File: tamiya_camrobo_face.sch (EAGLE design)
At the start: 21 parts, among them J4 AUDIO_JACK_3.5MM_KIT

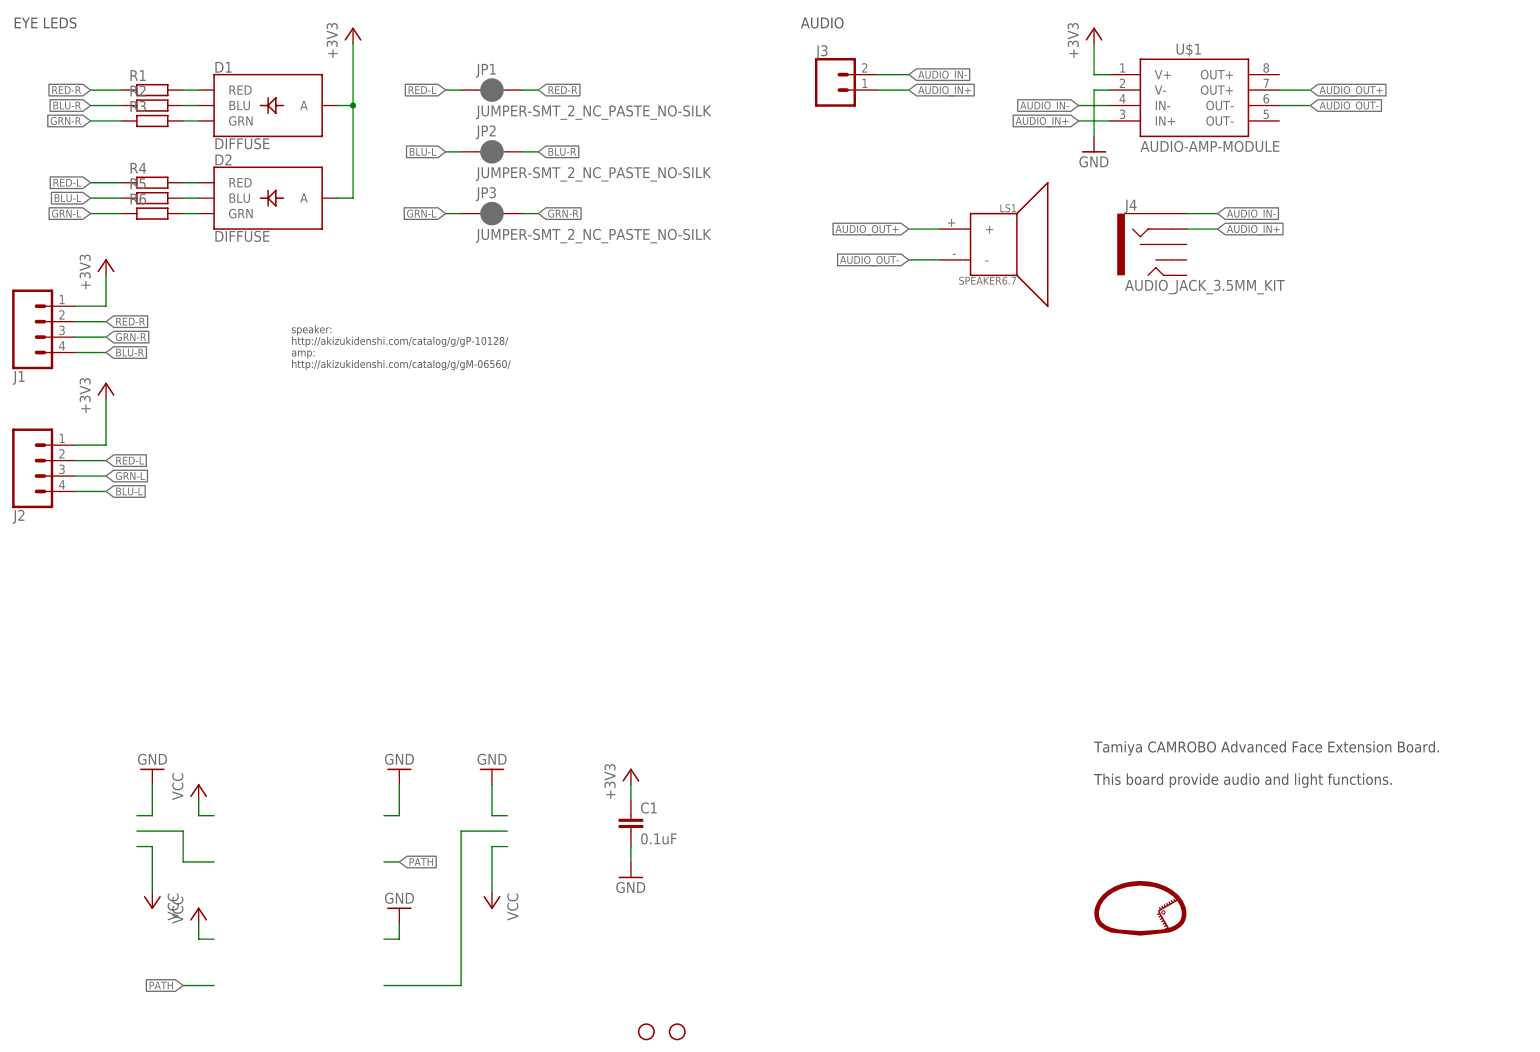
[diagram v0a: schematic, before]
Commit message: exchange led and amp
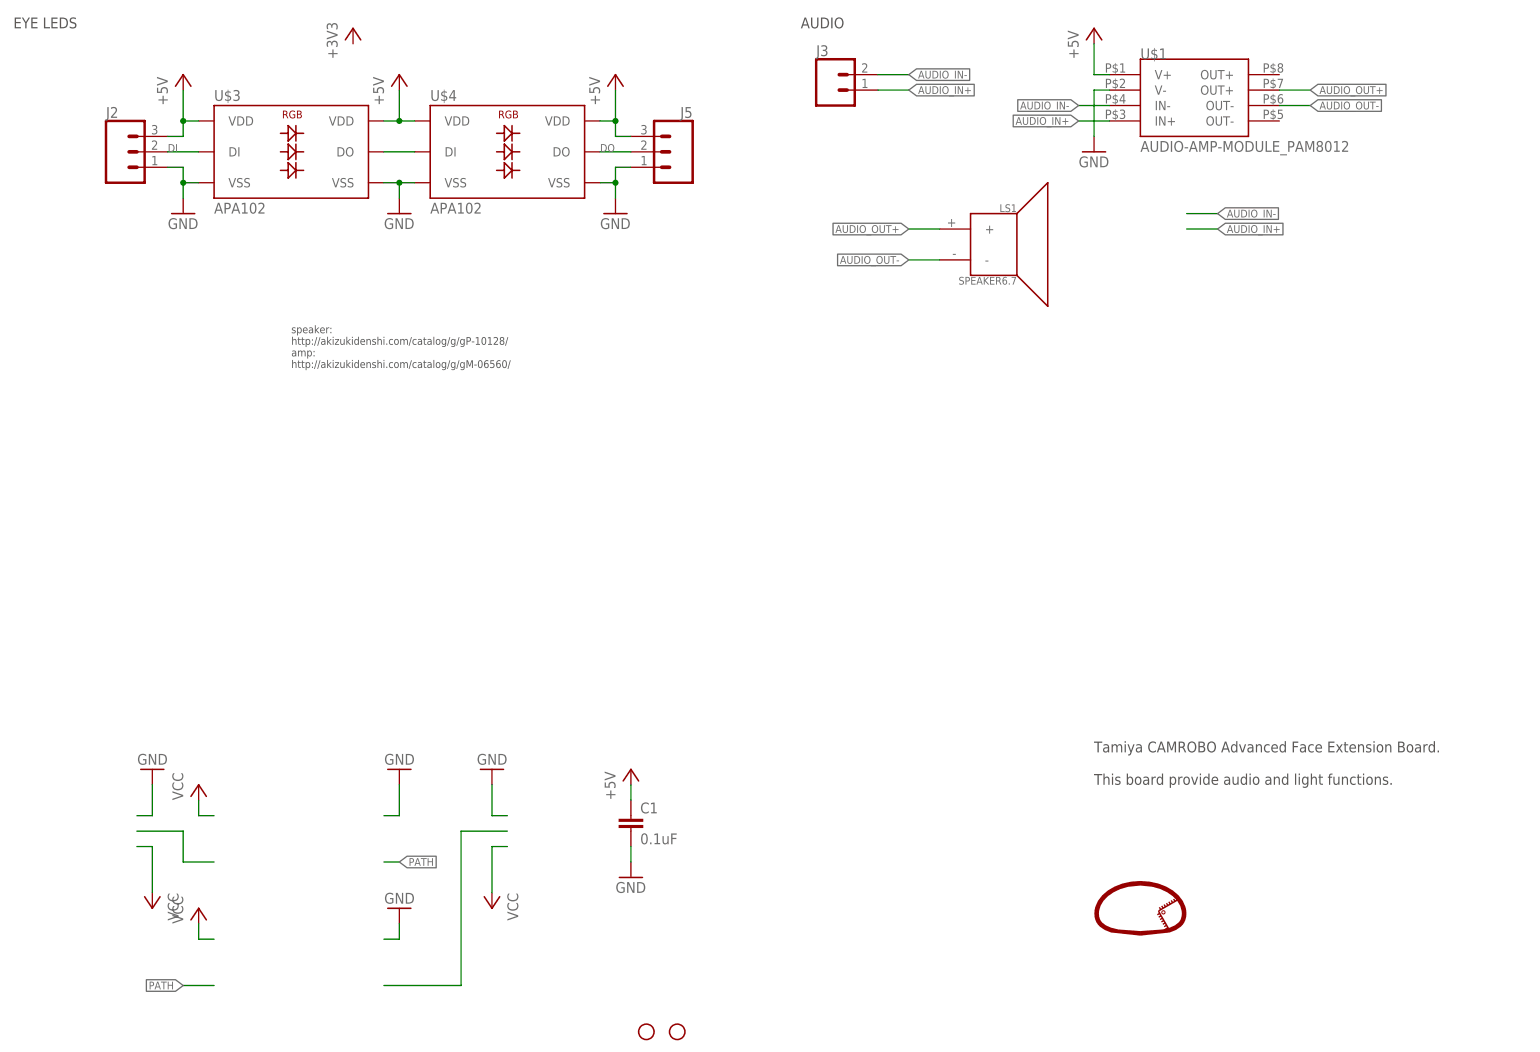
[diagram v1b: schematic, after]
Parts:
- removed D1, D2: DIFFUSE, SparkFun-LED:LED-RGB-CADIFFUSE
- removed J1: (no value), SparkFun-Connectors:CONN_04
- removed J4: AUDIO_JACK_3.5MM_KIT, SparkFun-Connectors:AUDIO_JACK_3.5MM_KIT
- removed JP1, JP2, JP3: JUMPER-SMT_2_NC_PASTE_NO-SILK, SparkFun-Jumpers:JUMPER-SMT_2_NC_PASTE_NO-SILK
- removed R1, R2, R3, R4, R5, R6: (no value), rcl:R-EU_0204/7
- added J5: (no value), SparkFun-Connectors:CONN_03
- added U$3, U$4: APA102, Botamochi-sensors:APA102
- J2: device SparkFun-Connectors:CONN_04 -> SparkFun-Connectors:CONN_03
- U$1: value AUDIO-AMP-MODULE -> AUDIO-AMP-MODULE_PAM8012; device Botamochi-sensors:AUDIO-AMP-MODULE -> Botamochi-sensors:AUDIO-AMP-MODULE_PAM8012
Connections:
- removed net +3V3: C1.1, D1.A, D2.A, J1.1, J2.1, U$1.V+
- removed net BLU-L: J2.4, JP2.1, R5.1
- removed net BLU-R: J1.4, JP2.2, R2.1
- removed net GRN-L: J2.3, JP3.1, R6.1
- removed net GRN-R: J1.3, JP3.2, R3.1
- removed net N$10: D2.GRN, R6.2
- removed net N$5: D1.RED, R1.2
- removed net N$6: D1.BLU, R2.2
- removed net N$7: D1.GRN, R3.2
- removed net N$8: D2.RED, R4.2
- removed net N$9: D2.BLU, R5.2
- removed net RED-L: J2.2, JP1.1, R4.1
- removed net RED-R: J1.2, JP1.2, R1.1
- new net +5V: C1.1, J2.3, J5.3, U$1.V+, U$3.VDD@1, U$3.VDD@2, U$4.VDD@1, U$4.VDD@2
- new net DI: J2.2, U$3.DI
- new net DO: J5.2, U$4.DO
- new net N$1: U$3.DO, U$4.DI
- net AUDIO_IN+: no longer J4.RING
- net AUDIO_IN-: no longer J4.SLEEVE
- net GND: now also J2.1, J5.1, U$3.VSS@1, U$3.VSS@2, U$4.VSS@1, U$4.VSS@2
